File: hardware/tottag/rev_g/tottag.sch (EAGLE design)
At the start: 194 parts, among them J1 USB4110-GF-A, J2 DM3AT-SF-PEJM5, J3 TC2030-JLINK-NL-2SIDE, J4 TC2030-JLINK-NL-2SIDE, J5 MOLEX-PICO-SPOX-3SIDE, Q1 CSD75207W15, Q4 CSD75207W15, T1 HHM1595A1, U1 DW1000, U10 STM32F091CC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

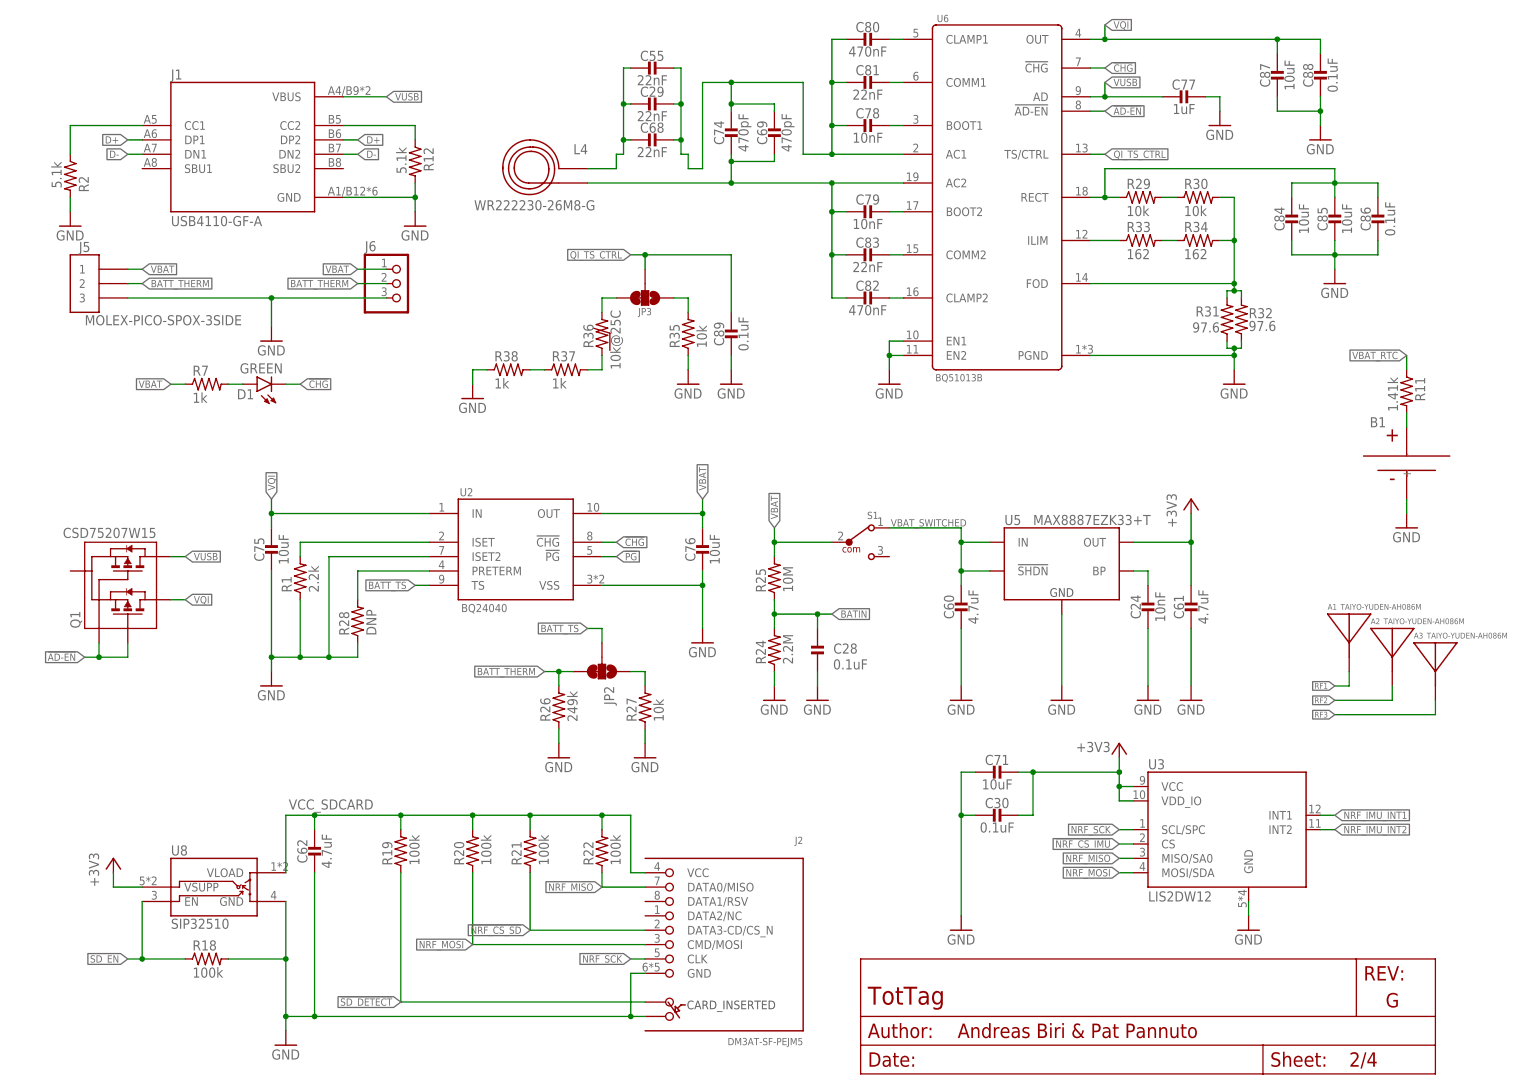
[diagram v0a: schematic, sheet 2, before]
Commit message: rev_g: design review fixes
 - Unify `!AD_EN` naming
 - C75/C76 10µF -> 1µF
 - Add battery pack details
 - Add NTC math details
 - Clarify switch on power diagram
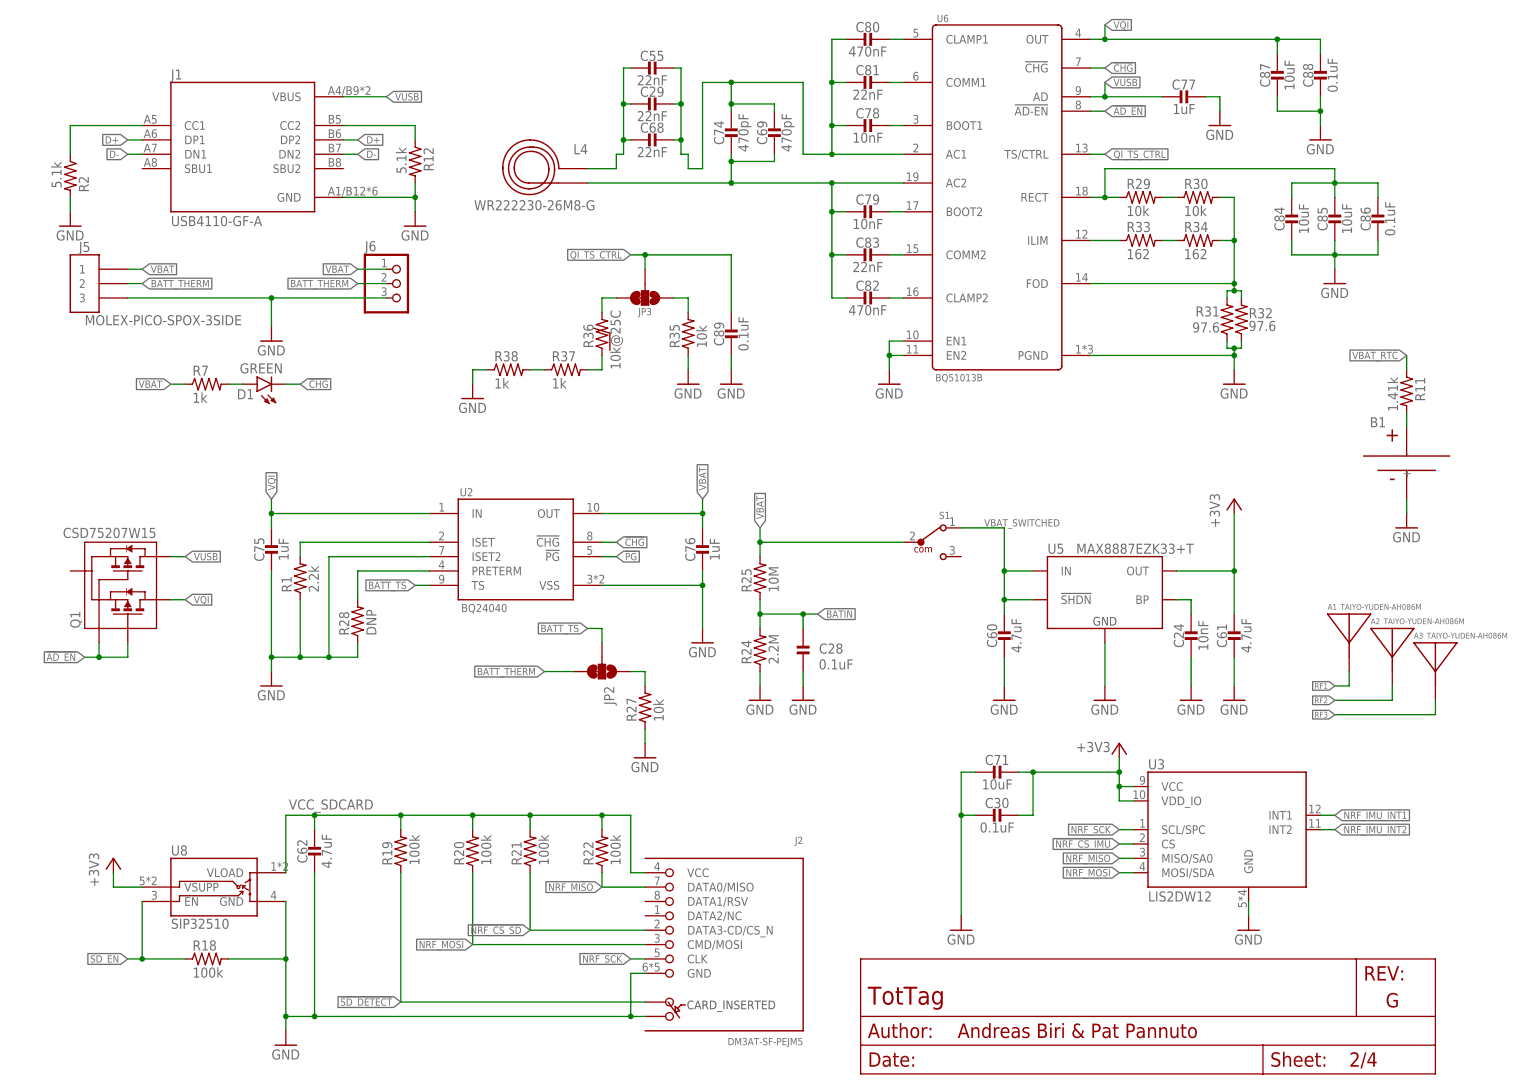
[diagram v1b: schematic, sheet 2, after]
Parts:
- removed R26: 249k, passives:RESISTOR0402_RES
- C75, C76: value 10uF -> 1uF; device passives:CAPACITOR0603_CAP -> passives:CAPACITOR0402_CAP; DIGIKEY 1253-CM105X5R106M25ATCT-ND -> 490-7195-1-ND; MPN CM105X5R106M25AT -> GRM155R70G105KA12D
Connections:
- net !AD-EN renamed !AD_EN
- net BATT_THERM: no longer R26.2
- net GND: no longer R26.1
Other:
- note added: "BATTERY HCP643450NZC, 3.7V, 1200mah Bare raw cell: 6.4*34.5*50.5mm max. in T*W*L Assemble size: 6.4*34.5*52 mm max. in T*W*L Over-charge voltage: 4.28V Over- discharge voltage: 3.0V Continuous charge rate: 0.2C Peck charge rate:1C Continuous discharge rate: 0.2C Peck discharge rate:1C, for 2-3ms NTC, 10K B=3435 Wire: UL1571-28AWG#, 100mm, from left Connector: MOLEX87439-3P, positive PCM added"
- note added: "Battery Monitoring"
- note added: "Datasheet wants a 10k NTC B=3370 Battery pack has a 10k NTC B=3435 At 0ºC: 1/273 = 1/298 + 1/3435 * ln(R/10000); R ~= 28.7 kΩ 1/273 = 1/298 + 1/3370 * ln(R/10000); R ~= 28.2 kΩ At 60ºC 1/333 = 1/298 + 1/3435 * ln(R/10000); R ~= 2.98 kΩ 1/333 = 1/298 + 1/3370 * ln(R/10000); R ~= 3.05 kΩ Close enough."
- note added: "Main Power Switch"
- note removed: "Battery monitoring"
- note removed: "Datasheet wants "103AT" NTC --- 103 = 10k AT = "High-precision" (1% tol?) --- Battery pack has 10k NTC with B=3435k --- That matches the B of first few 103AT datasheets; must be a thing"
- moved on the sheet: C24, C28, C60, C61, R24, R25, S1, U5

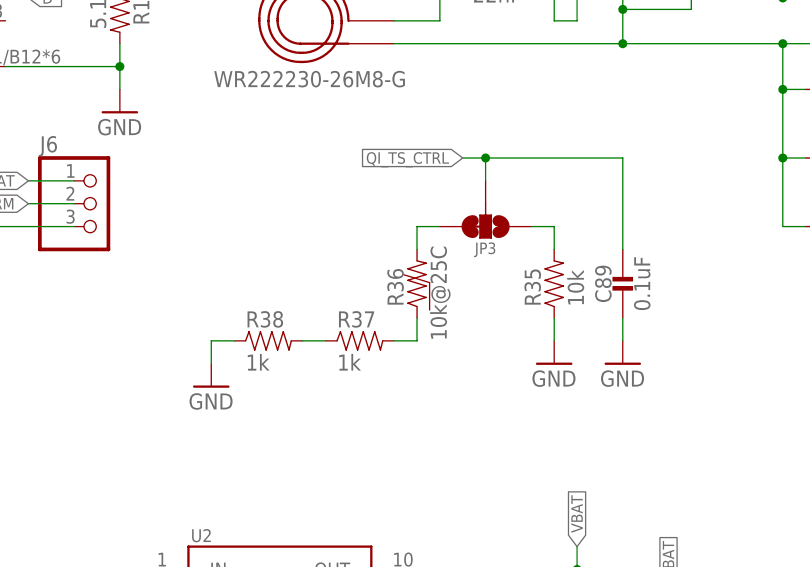
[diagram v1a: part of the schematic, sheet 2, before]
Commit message: rev_g: correct thermistor prefix (R36 -> RT1)
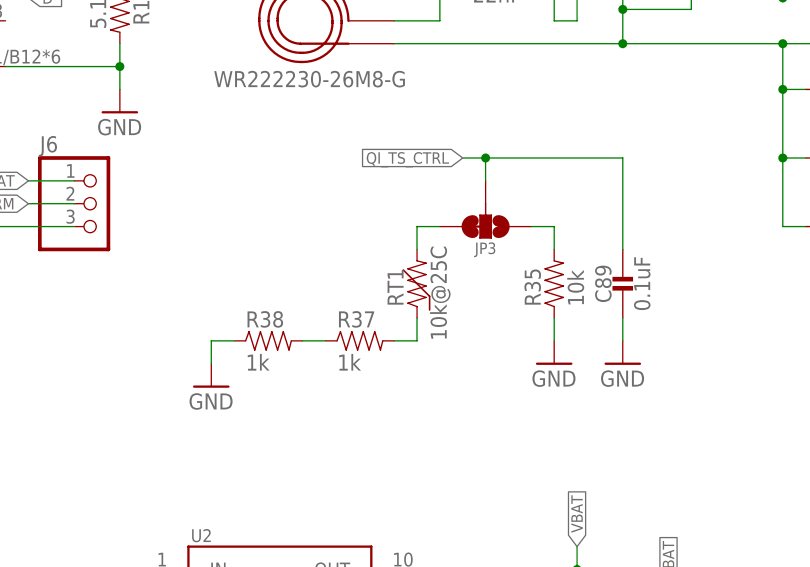
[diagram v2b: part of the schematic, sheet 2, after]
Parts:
- renumbered R36 to RT1
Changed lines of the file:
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@@
 </part>
 <part name="SUPPLY37" library="supply1" library_urn="urn:adsk.eagle:library:371" deviceset="GND" device=""/>
-<part name="R36" library="passives" library_urn="urn:adsk.eagle:library:20904581" deviceset="THERMISTOR" device="0402" package3d_urn="urn:adsk.eagle:package:20904668/2" value="10k@25C"/>
+<part name="RT1" library="passives" library_urn="urn:adsk.eagle:library:20904581" deviceset="THERMISTOR" device="0402" package3d_urn="urn:adsk.eagle:package:20904668/2" value="10k@25C"/>
 <part name="SUPPLY38" library="supply1" library_urn="urn:adsk.eagle:library:371" deviceset="GND" device=""/>
 <part name="C89" library="passives" deviceset="CAPACITOR" device="0402_CAP" value="0.1uF">
@@
 <attribute name="VALUE" x="114.3" y="119.38" size="1.778" layer="96"/>
 </instance>
-<instance part="R36" gate="B" x="101.6" y="132.08" smashed="yes" rot="R90">
+<instance part="RT1" gate="B" x="101.6" y="132.08" smashed="yes" rot="R90">
 <attribute name="NAME" x="100.1014" y="128.27" size="1.778" layer="95" rot="R90"/>
 <attribute name="VALUE" x="104.902" y="124.46" size="1.778" layer="96" rot="R90"/>
@@
 <segment>
 <pinref part="JP3" gate="G$1" pin="3"/>
-<pinref part="R36" gate="B" pin="2"/>
+<pinref part="RT1" gate="B" pin="2"/>
 <wire x1="104.14" y1="137.16" x2="101.6" y2="137.16" width="0.1524" layer="91"/>
 <wire x1="101.6" y1="137.16" x2="101.6" y2="134.62" width="0.1524" layer="91"/>
@@
 <net name="N$69" class="0">
 <segment>
-<pinref part="R36" gate="B" pin="1"/>
+<pinref part="RT1" gate="B" pin="1"/>
 <pinref part="R37" gate="G$1" pin="2"/>
 <wire x1="101.6" y1="127" x2="101.6" y2="124.46" width="0.1524" layer="91"/>

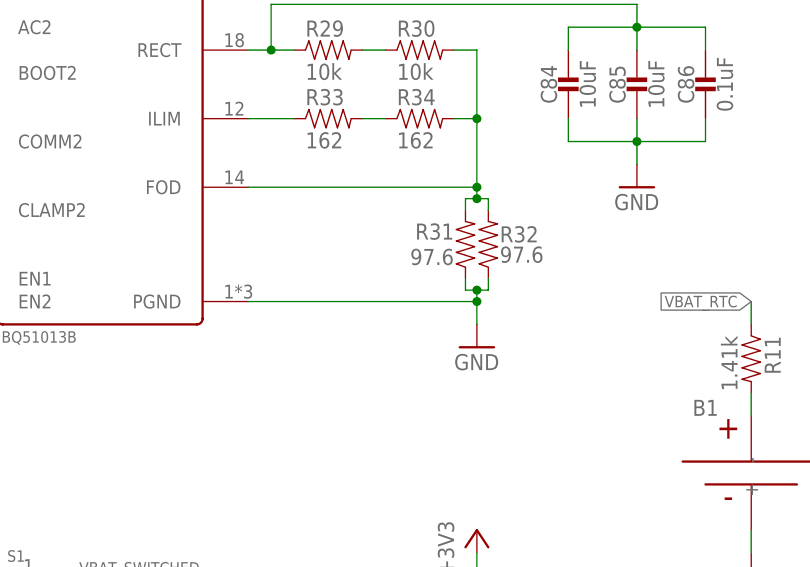
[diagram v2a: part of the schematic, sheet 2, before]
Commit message: rev_g: Fix R31, R32 series / parallel
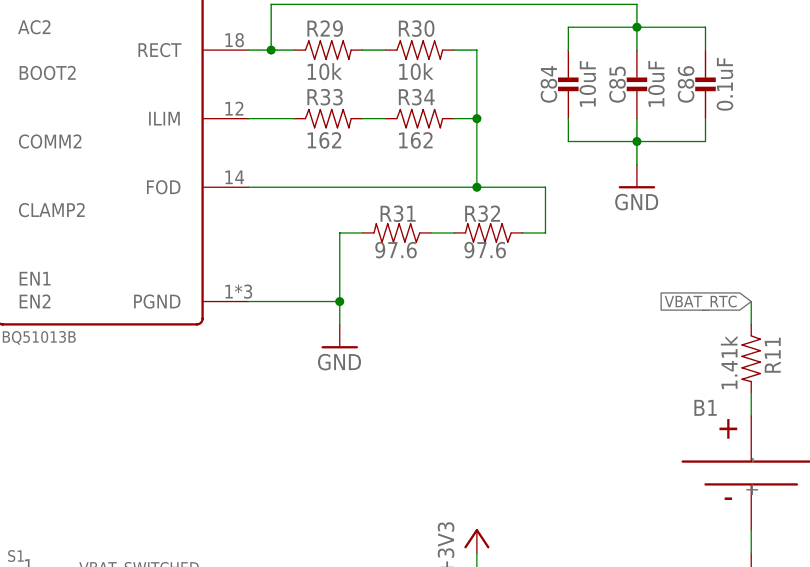
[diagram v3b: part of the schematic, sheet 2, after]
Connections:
- new net N$28: R31.1, R32.2
- net BQ_FOD: now also R32.1; no longer R31.2, R32.2
- net GND: now also R31.2; no longer R31.1, R32.1
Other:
- moved on the sheet: R31, R32
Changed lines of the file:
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@@
 <wire x1="135.89" y1="173.99" x2="135.89" y2="158.75" width="0.127" layer="98" style="shortdash"/>
 <text x="130.048" y="173.228" size="1.016" layer="98" align="top-center">"C2" in ref design</text>
-<text x="201.93" y="136.144" size="0.8128" layer="98" align="top-right">Set to 196Ω
+<text x="197.358" y="137.668" size="0.8128" layer="98" align="top-right">Set to 196Ω
 per EVM rec.
 Do with two R's
@@
 <attribute name="VALUE" x="160.528" y="123.698" size="1.27" layer="96" font="vector" ratio="12" align="top-left"/>
 </instance>
-<instance part="SUPPLY32" gate="1" x="213.36" y="121.92" smashed="yes">
-<attribute name="VALUE" x="210.82" y="119.38" size="1.778" layer="96"/>
+<instance part="SUPPLY32" gate="1" x="198.12" y="121.92" smashed="yes">
+<attribute name="VALUE" x="195.58" y="119.38" size="1.778" layer="96"/>
 </instance>
 <instance part="C77" gate="G$1" x="205.74" y="172.72" smashed="yes" rot="R270">
@@
 <attribute name="VALUE" x="208.28" y="165.1" size="1.778" layer="96"/>
 </instance>
-<instance part="R31" gate="G$1" x="212.09" y="134.62" smashed="yes" rot="R90">
-<attribute name="NAME" x="210.82" y="135.6614" size="1.778" layer="95" rot="R180"/>
-<attribute name="VALUE" x="210.82" y="132.842" size="1.778" layer="96" rot="R180"/>
-<attribute name="DIGIKEY" x="212.09" y="134.62" size="1.27" layer="96" rot="R90" align="top-left" display="off"/>
-<attribute name="MPN" x="212.09" y="134.62" size="1.27" layer="96" rot="R90" align="top-left" display="off"/>
-</instance>
-<instance part="R32" gate="G$1" x="214.63" y="134.62" smashed="yes" rot="R90">
-<attribute name="NAME" x="215.9" y="133.5786" size="1.778" layer="95"/>
-<attribute name="VALUE" x="215.9" y="131.318" size="1.778" layer="96"/>
-<attribute name="DIGIKEY" x="214.63" y="134.62" size="1.27" layer="96" rot="R90" align="top-left" display="off"/>
-<attribute name="MPN" x="214.63" y="134.62" size="1.27" layer="96" rot="R90" align="top-left" display="off"/>
+<instance part="R31" gate="G$1" x="203.2" y="134.62" smashed="yes" rot="R180">
+<attribute name="NAME" x="202.438" y="135.8646" size="1.778" layer="95"/>
+<attribute name="VALUE" x="201.93" y="131.826" size="1.778" layer="96"/>
+<attribute name="DIGIKEY" x="203.2" y="134.62" size="1.27" layer="96" rot="R180" align="top-left" display="off"/>
+<attribute name="MPN" x="203.2" y="134.62" size="1.27" layer="96" rot="R180" align="top-left" display="off"/>
+</instance>
+<instance part="R32" gate="G$1" x="213.36" y="134.62" smashed="yes" rot="R180">
+<attribute name="NAME" x="211.836" y="135.8646" size="1.778" layer="95"/>
+<attribute name="VALUE" x="211.836" y="131.826" size="1.778" layer="96"/>
+<attribute name="DIGIKEY" x="213.36" y="134.62" size="1.27" layer="96" rot="R180" align="top-left" display="off"/>
+<attribute name="MPN" x="213.36" y="134.62" size="1.27" layer="96" rot="R180" align="top-left" display="off"/>
 </instance>
 <instance part="R33" gate="G$1" x="198.12" y="147.32" smashed="yes">
@@
 <pinref part="U6" gate="B" pin="PGND"/>
 <pinref part="SUPPLY32" gate="1" pin="GND"/>
-<wire x1="187.96" y1="127" x2="213.36" y2="127" width="0.1524" layer="91"/>
-<wire x1="213.36" y1="127" x2="213.36" y2="124.46" width="0.1524" layer="91"/>
-<pinref part="R31" gate="G$1" pin="1"/>
-<wire x1="212.09" y1="129.54" x2="212.09" y2="128.27" width="0.1524" layer="91"/>
-<pinref part="R32" gate="G$1" pin="1"/>
-<wire x1="212.09" y1="128.27" x2="213.36" y2="128.27" width="0.1524" layer="91"/>
-<wire x1="213.36" y1="128.27" x2="214.63" y2="128.27" width="0.1524" layer="91"/>
-<wire x1="214.63" y1="128.27" x2="214.63" y2="129.54" width="0.1524" layer="91"/>
-<wire x1="213.36" y1="127" x2="213.36" y2="128.27" width="0.1524" layer="91"/>
-<junction x="213.36" y="127"/>
-<junction x="213.36" y="128.27"/>
+<wire x1="187.96" y1="127" x2="198.12" y2="127" width="0.1524" layer="91"/>
+<wire x1="198.12" y1="127" x2="198.12" y2="124.46" width="0.1524" layer="91"/>
+<pinref part="R31" gate="G$1" pin="2"/>
+<wire x1="200.66" y1="134.62" x2="198.12" y2="134.62" width="0.1524" layer="91"/>
+<wire x1="198.12" y1="134.62" x2="198.12" y2="127" width="0.1524" layer="91"/>
+<junction x="198.12" y="127"/>
 </segment>
 <segment>
@@
 <net name="BQ_FOD" class="0">
 <segment>
-<pinref part="R31" gate="G$1" pin="2"/>
-<wire x1="212.09" y1="137.16" x2="212.09" y2="138.43" width="0.1524" layer="91"/>
-<pinref part="R32" gate="G$1" pin="2"/>
-<wire x1="212.09" y1="138.43" x2="213.36" y2="138.43" width="0.1524" layer="91"/>
-<wire x1="213.36" y1="138.43" x2="214.63" y2="138.43" width="0.1524" layer="91"/>
-<wire x1="214.63" y1="138.43" x2="214.63" y2="137.16" width="0.1524" layer="91"/>
-<wire x1="213.36" y1="138.43" x2="213.36" y2="139.7" width="0.1524" layer="91"/>
-<junction x="213.36" y="138.43"/>
 <pinref part="U6" gate="B" pin="FOD"/>
 <wire x1="187.96" y1="139.7" x2="213.36" y2="139.7" width="0.1524" layer="91"/>
@@
 <wire x1="210.82" y1="154.94" x2="213.36" y2="154.94" width="0.1524" layer="91"/>
 <wire x1="213.36" y1="154.94" x2="213.36" y2="147.32" width="0.1524" layer="91"/>
-<junction x="213.36" y="139.7"/>
 <wire x1="213.36" y1="147.32" x2="213.36" y2="139.7" width="0.1524" layer="91"/>
 <wire x1="210.82" y1="147.32" x2="213.36" y2="147.32" width="0.1524" layer="91"/>
 <junction x="213.36" y="147.32"/>
 <pinref part="R34" gate="G$1" pin="2"/>
+<pinref part="R32" gate="G$1" pin="1"/>
+<wire x1="218.44" y1="134.62" x2="220.98" y2="134.62" width="0.1524" layer="91"/>
+<wire x1="220.98" y1="134.62" x2="220.98" y2="139.7" width="0.1524" layer="91"/>
+<wire x1="220.98" y1="139.7" x2="213.36" y2="139.7" width="0.1524" layer="91"/>
+<junction x="213.36" y="139.7"/>
 </segment>
 </net>
@@
 </segment>
 </net>
+<net name="N$28" class="0">
+<segment>
+<pinref part="R31" gate="G$1" pin="1"/>
+<pinref part="R32" gate="G$1" pin="2"/>
+<wire x1="208.28" y1="134.62" x2="210.82" y2="134.62" width="0.1524" layer="91"/>
+</segment>
+</net>
